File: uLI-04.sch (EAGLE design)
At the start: 38 parts, among them IC1 PIC18F14K50-I/SS, IC2 ADM2483, IC4 78L05F, J1 PICPROG2-V, J5 WEBP6-4, J6 WEBP6-4, J7 WEBP6-4, Q1 12.00 MHz, T1 IRF7306, X1 MINI-USB_SHIELD4P-USB-SPEC, X2 ARK1550/2_S

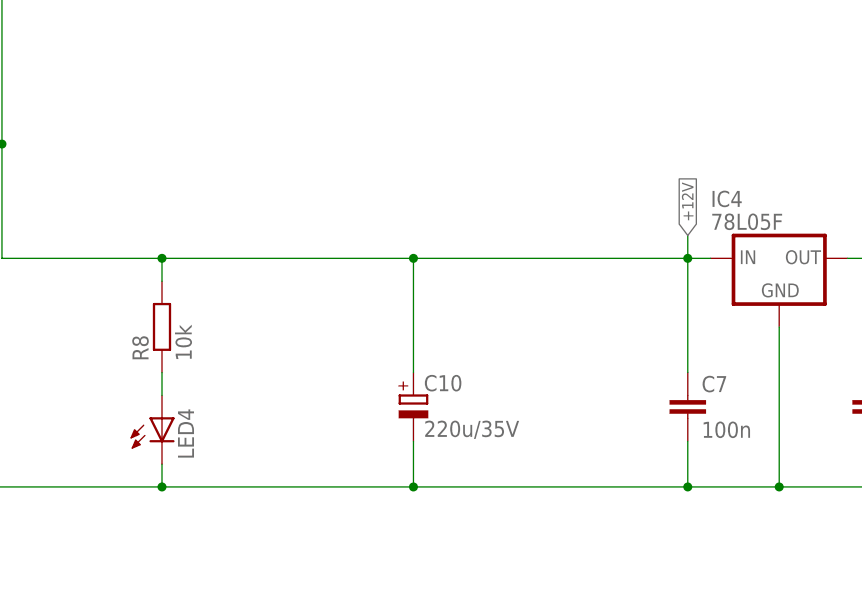
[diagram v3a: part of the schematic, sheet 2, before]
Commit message: Omezeni proudovych razu - schema
Pridan na schema rezistor a zmensen kondenzator pred stabilizator.
Editovano jen schema. Deska neupravena.
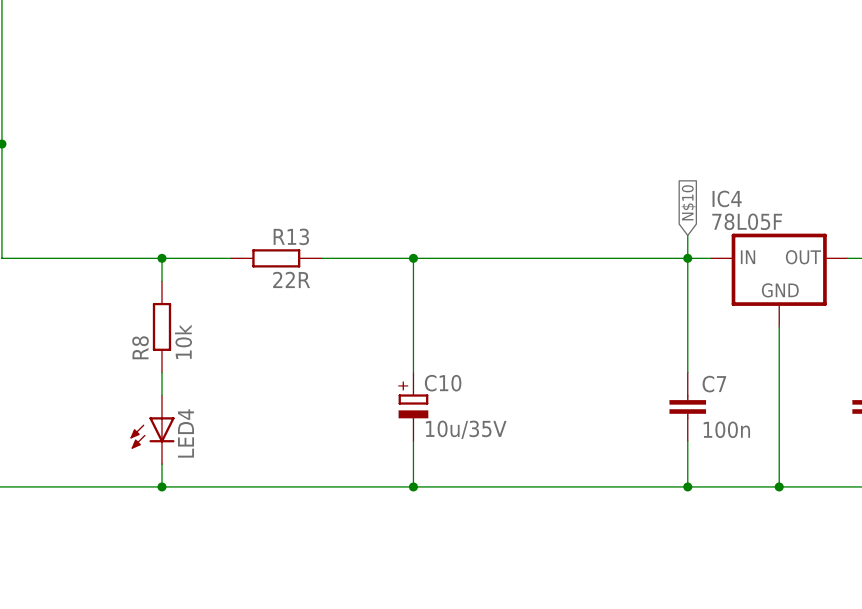
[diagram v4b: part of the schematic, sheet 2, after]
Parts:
- added R13: 22R, rcl:R-EU_R1206
- C10: value 220u/35V -> 10u/35V; device rcl:CPOL-EUE3.5-8 -> rcl:CPOL-EUE2-5
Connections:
- new net N$10: C10.+, C7.1, IC4.VI, R13.1
- net +12V: now also R13.2; no longer C10.+, C7.1, IC4.VI

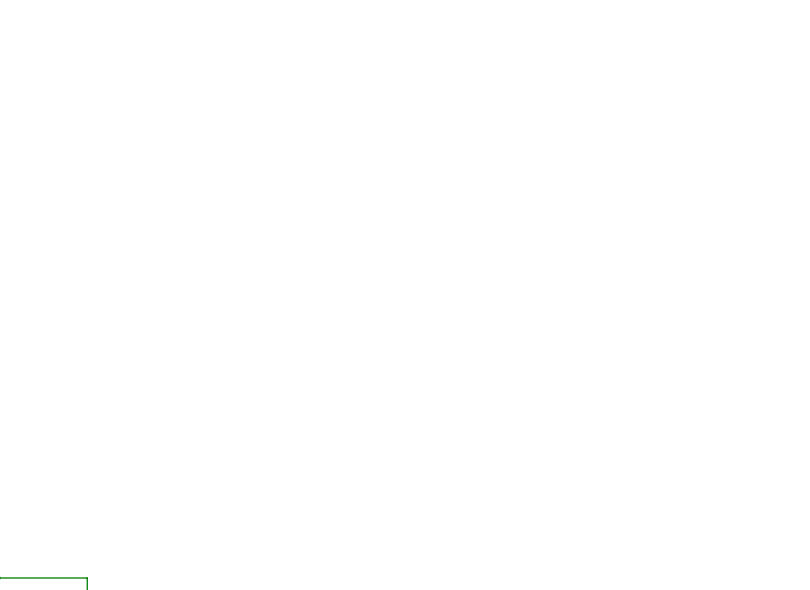
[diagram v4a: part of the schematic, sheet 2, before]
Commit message: Pridan brown-out reset pro PV pin
Jen schema.
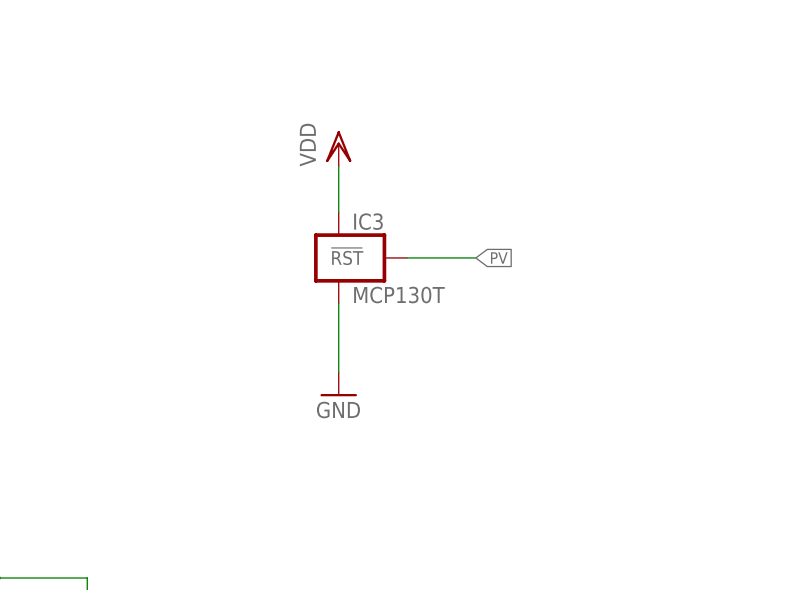
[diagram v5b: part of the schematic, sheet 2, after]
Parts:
- removed R12: OR, rcl:R-EU_R1206
- added IC3: MCP130T, my:MCP130T
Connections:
- removed net N$8: IC2.PV, R12.1
- new net PV: IC2.PV, IC3.!RST
- net GND: now also IC3.GND
- net VDD: now also IC3.VCC; no longer R12.2

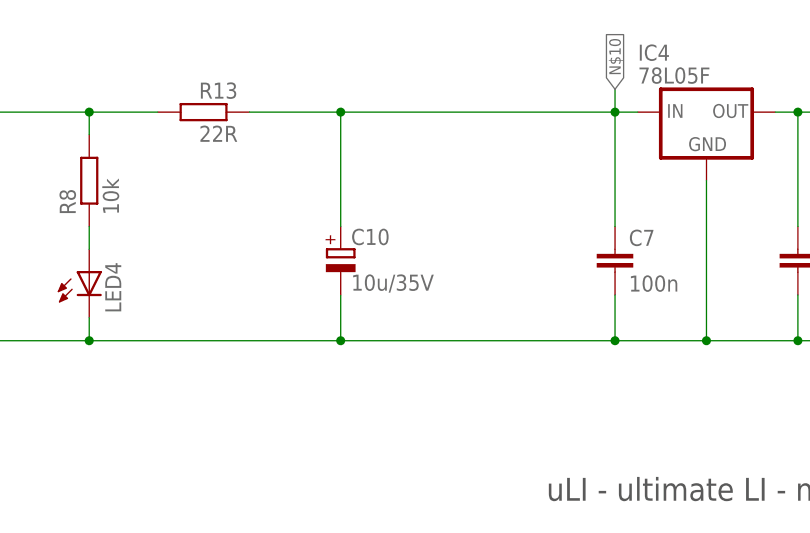
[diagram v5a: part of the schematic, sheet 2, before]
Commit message: Upravena hodnota kondenzatoru XN na 22uF.
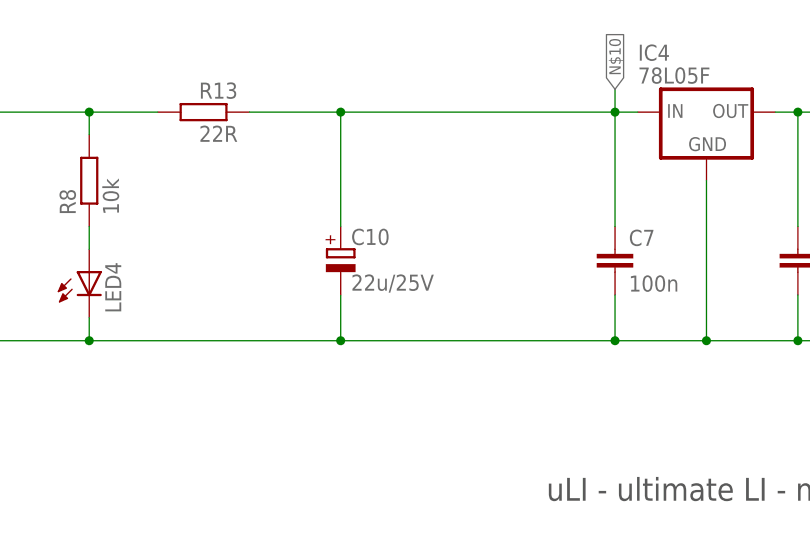
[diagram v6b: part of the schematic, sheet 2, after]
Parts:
- C10: value 10u/35V -> 22u/25V
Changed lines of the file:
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@@
 <part name="R10" library="rcl" deviceset="R-EU_" device="R1206" value="100k"/>
 <part name="T1" library="transistor-fet" deviceset="IRF7306" device=""/>
-<part name="C10" library="rcl" deviceset="CPOL-EU" device="E2-5" value="10u/35V"/>
+<part name="C10" library="rcl" deviceset="CPOL-EU" device="E2-5" value="22u/25V"/>
 <part name="J5" library="con-malina" deviceset="WEBP6-4" device="_SHORT" value="WEBP6-4">
 <variant name="slave" populate="no"/>
